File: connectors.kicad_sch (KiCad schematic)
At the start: 4 parts, among them J1 Conn_01x04_Pin, J2 Conn_01x04_Pin, J3 Conn_01x09_Pin, J4 Conn_02x03_Odd_Even

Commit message: Completed symbols to footprints associations
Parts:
- J1, J2: footprint (none) -> Connector_PinHeader_2.54mm:PinHeader_1x04_P2.54mm_Vertical
- J3: footprint (none) -> Connector_PinHeader_2.54mm:PinHeader_1x09_P2.54mm_Vertical
- J4: footprint (none) -> Connector_PinHeader_2.54mm:PinHeader_2x03_P2.54mm_Vertical
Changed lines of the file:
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@@
 			)
 		)
-		(property "Footprint" ""
+		(property "Footprint" "Connector_PinHeader_2.54mm:PinHeader_2x03_P2.54mm_Vertical"
 			(at 88.9 83.82 0)
 			(effects
@@
 			)
 		)
-		(property "Footprint" ""
+		(property "Footprint" "Connector_PinHeader_2.54mm:PinHeader_1x09_P2.54mm_Vertical"
 			(at 68.58 87.63 0)
 			(effects
@@
 			)
 		)
-		(property "Footprint" ""
+		(property "Footprint" "Connector_PinHeader_2.54mm:PinHeader_1x04_P2.54mm_Vertical"
 			(at 86.36 62.23 0)
 			(effects
@@
 			)
 		)
-		(property "Footprint" ""
+		(property "Footprint" "Connector_PinHeader_2.54mm:PinHeader_1x04_P2.54mm_Vertical"
 			(at 68.58 60.96 0)
 			(effects

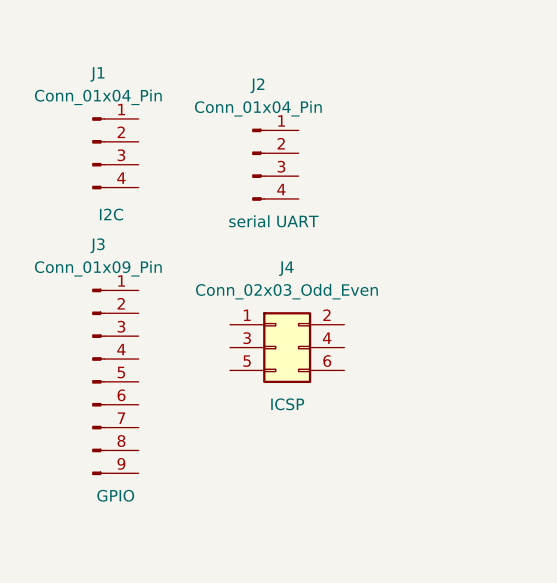
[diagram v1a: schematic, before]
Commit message: Completed wirings for connector sheet
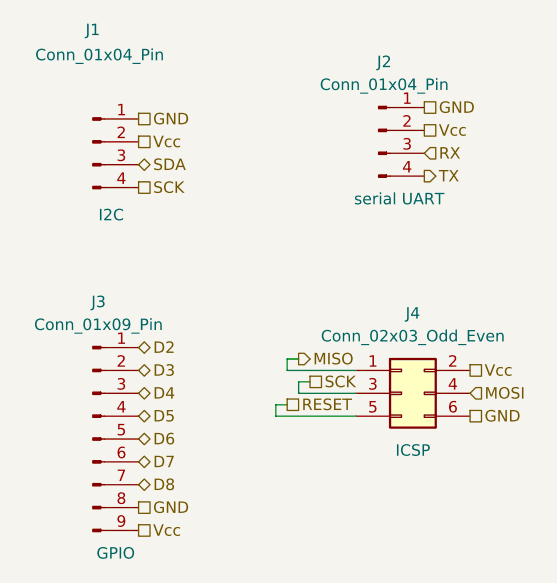
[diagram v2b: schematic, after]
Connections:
- net MISO: now reaches J4.1 (Pin_1)
- net Vcc: now reaches J4.2 (Pin_2)
- net Vcc: now also J1.2 (Pin_2), J2.2 (Pin_2), J3.9 (Pin_9)
- net SCK: now reaches J4.3 (Pin_3)
- net SCK: now also J1.4 (Pin_4)
- net MOSI: now reaches J4.4 (Pin_4)
- net RESET: now reaches J4.5 (Pin_5)
- net GND: now reaches J4.6 (Pin_6)
- net GND: now also J1.1 (Pin_1), J2.1 (Pin_1), J3.8 (Pin_8)
- net D2: now reaches J3.1 (Pin_1)
- net D3: now reaches J3.2 (Pin_2)
- net D4: now reaches J3.3 (Pin_3)
- net D5: now reaches J3.4 (Pin_4)
- net D6: now reaches J3.5 (Pin_5)
- net D7: now reaches J3.6 (Pin_6)
- net D8: now reaches J3.7 (Pin_7)
- net RX: now reaches J2.3 (Pin_3)
- net TX: now reaches J2.4 (Pin_4)
- net SDA: now reaches J1.3 (Pin_3)
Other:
- moved on the sheet: J2, J3, J4
